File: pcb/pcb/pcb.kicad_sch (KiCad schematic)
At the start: 24 parts, among them J1 UART, J2 Barrel_Jack, J3 Stepper, SW1 RESET, SW2 FLASH, U1 ESP32-WROOM-32, U2 TSR_1-2433

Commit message: third reddit revision
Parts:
- L1: footprint Inductor_SMD:L_1206_3216Metric_Pad1.22x1.90mm_HandSolder -> Inductor_SMD:L_TracoPower_TCK-141
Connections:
- net A1: now also J3.2 (Pin_2); no longer J3.3 (Pin_3)
- net A2: now also J3.1 (Pin_1); no longer J3.4 (Pin_4)
- net B1: now also J3.3 (Pin_3); no longer J3.2 (Pin_2)
- net B2: now also J3.4 (Pin_4); no longer J3.1 (Pin_1)
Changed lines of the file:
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@@
   (title_block
     (title "twilight")
-    (date "2022-01-28")
+    (date "2022-01-30")
     (rev "1.0")
     (comment 4 "ESP32 and DRV8825 based stepper motor controller")
@@
     (property "Reference" "L1" (id 0) (at 194.31 39.37 90))
     (property "Value" "5.6uH" (id 1) (at 194.31 41.91 90))
-    (property "Footprint" "Inductor_SMD:L_1206_3216Metric_Pad1.22x1.90mm_HandSolder" (id 2) (at 194.31 45.72 0)
+    (property "Footprint" "Inductor_SMD:L_TracoPower_TCK-141" (id 2) (at 194.31 45.72 0)
       (effects (font (size 1.27 1.27)) hide)
     )
@@
     (pin "2")
   )
-  (symbol (lib_id "Connector_Generic:Conn_01x04") (at 215.9 129.54 0) (mirror x) (unit 1)
-    (in_bom yes) (on_board yes) (fields_autoplaced)
-    (property "Reference" "J3" (id 0) (at 215.9 118.11 0))
-    (property "Value" "Stepper" (id 1) (at 215.9 120.65 0))
-    (property "Footprint" "Connector_PinHeader_2.54mm:PinHeader_1x04_P2.54mm_Horizontal" (id 2) (at 215.9 129.54 0)
-      (effects (font (size 1.27 1.27)) hide)
-    )
-    (property "Datasheet" "~" (id 3) (at 215.9 129.54 0)
+  (symbol (lib_id "Connector_Generic:Conn_01x04") (at 215.9 127 0) (unit 1)
+    (in_bom yes) (on_board yes) (fields_autoplaced)
+    (property "Reference" "J3" (id 0) (at 218.44 126.9999 0)
+      (effects (font (size 1.27 1.27)) (justify left))
+    )
+    (property "Value" "Stepper" (id 1) (at 218.44 129.5399 0)
+      (effects (font (size 1.27 1.27)) (justify left))
+    )
+    (property "Footprint" "Connector_PinHeader_2.54mm:PinHeader_1x04_P2.54mm_Horizontal" (id 2) (at 215.9 127 0)
+      (effects (font (size 1.27 1.27)) hide)
+    )
+    (property "Datasheet" "~" (id 3) (at 215.9 127 0)
       (effects (font (size 1.27 1.27)) hide)
     )
@@
     )
     (path "/6243677a-61f4-42bd-9218-5496f7fcebdc"
-      (reference "L1") (unit 1) (value "5.6uH") (footprint "Inductor_SMD:L_1206_3216Metric_Pad1.22x1.90mm_HandSolder")
+      (reference "L1") (unit 1) (value "5.6uH") (footprint "Inductor_SMD:L_TracoPower_TCK-141")
     )
     (path "/618b85b8-3878-4dca-95c1-d1249ea332c0"

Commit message: fix mounting hole footprint in schematic
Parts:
- H1, H3: footprint MountingHole:MountingHole_3.2mm_M3_Pad -> MountingHole:MountingHole_3.2mm_M3
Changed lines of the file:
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@@
       (effects (font (size 1.27 1.27)) (justify left))
     )
-    (property "Footprint" "MountingHole:MountingHole_3.2mm_M3_Pad" (id 2) (at 34.29 27.94 0)
+    (property "Footprint" "MountingHole:MountingHole_3.2mm_M3" (id 2) (at 34.29 27.94 0)
       (effects (font (size 1.27 1.27)) hide)
     )
@@
       (effects (font (size 1.27 1.27)) (justify left))
     )
-    (property "Footprint" "MountingHole:MountingHole_3.2mm_M3_Pad" (id 2) (at 69.85 27.94 0)
+    (property "Footprint" "MountingHole:MountingHole_3.2mm_M3" (id 2) (at 69.85 27.94 0)
       (effects (font (size 1.27 1.27)) hide)
     )
@@
     )
     (path "/34fa3d54-c535-425c-b022-e1943d8d5f86"
-      (reference "H1") (unit 1) (value "MountingHole") (footprint "MountingHole:MountingHole_3.2mm_M3_Pad")
+      (reference "H1") (unit 1) (value "MountingHole") (footprint "MountingHole:MountingHole_3.2mm_M3")
     )
     (path "/00d9b647-6f7b-4061-b8f8-f07282eb45d6"
@@
     )
     (path "/72d1a3aa-0e7b-4b10-a84c-7a0d93e80db5"
-      (reference "H3") (unit 1) (value "MountingHole") (footprint "MountingHole:MountingHole_3.2mm_M3_Pad")
+      (reference "H3") (unit 1) (value "MountingHole") (footprint "MountingHole:MountingHole_3.2mm_M3")
     )
     (path "/b3ffd185-6873-4234-b901-27672efba3ad"

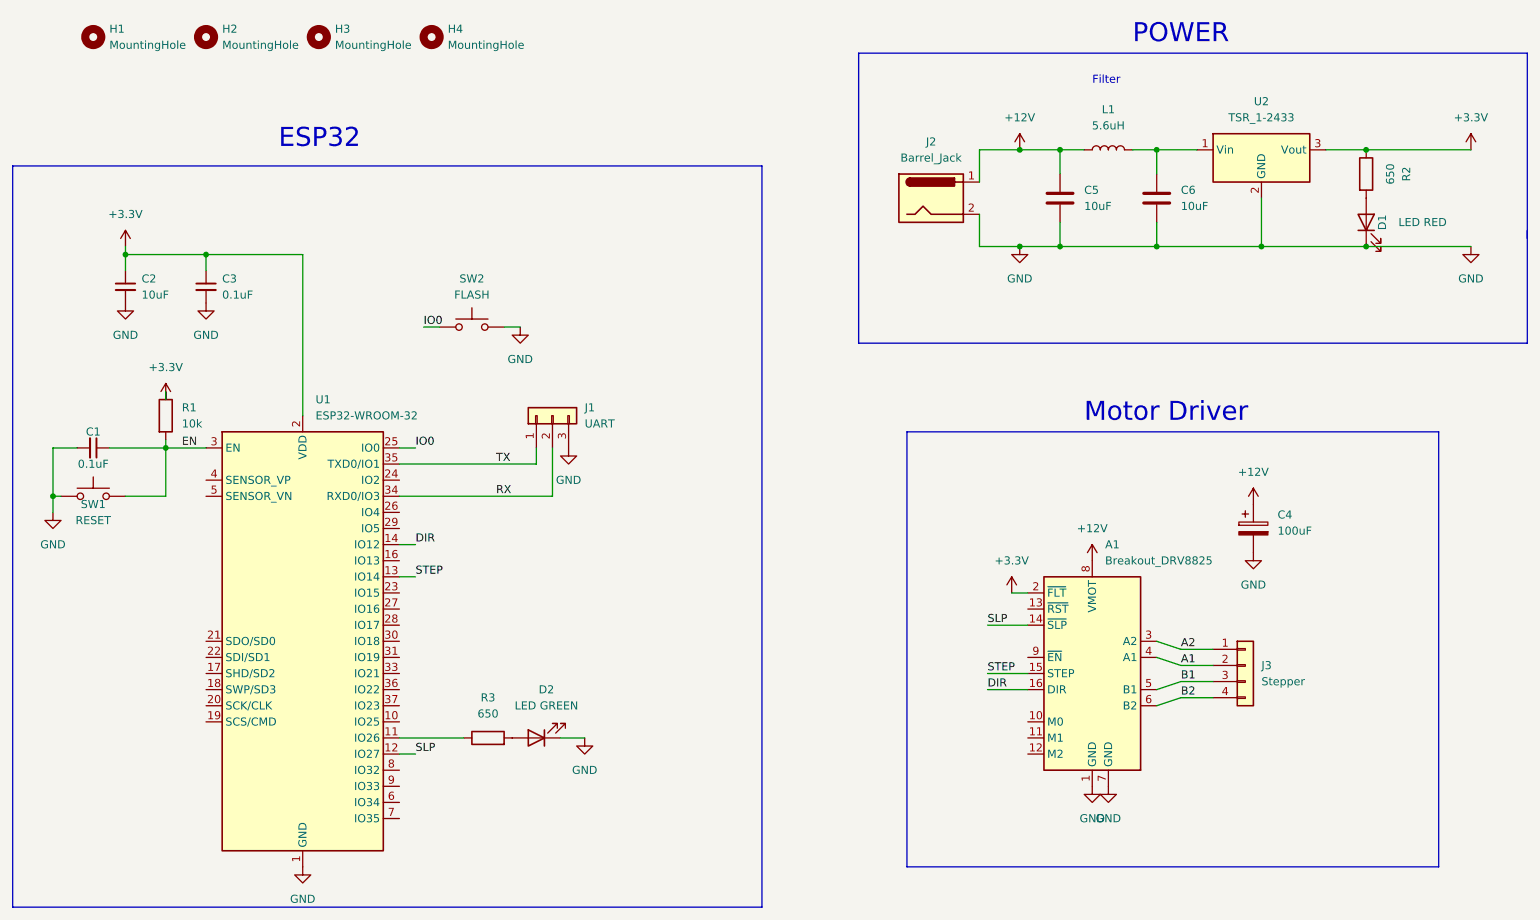
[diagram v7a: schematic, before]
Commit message: change resistor values to more standard
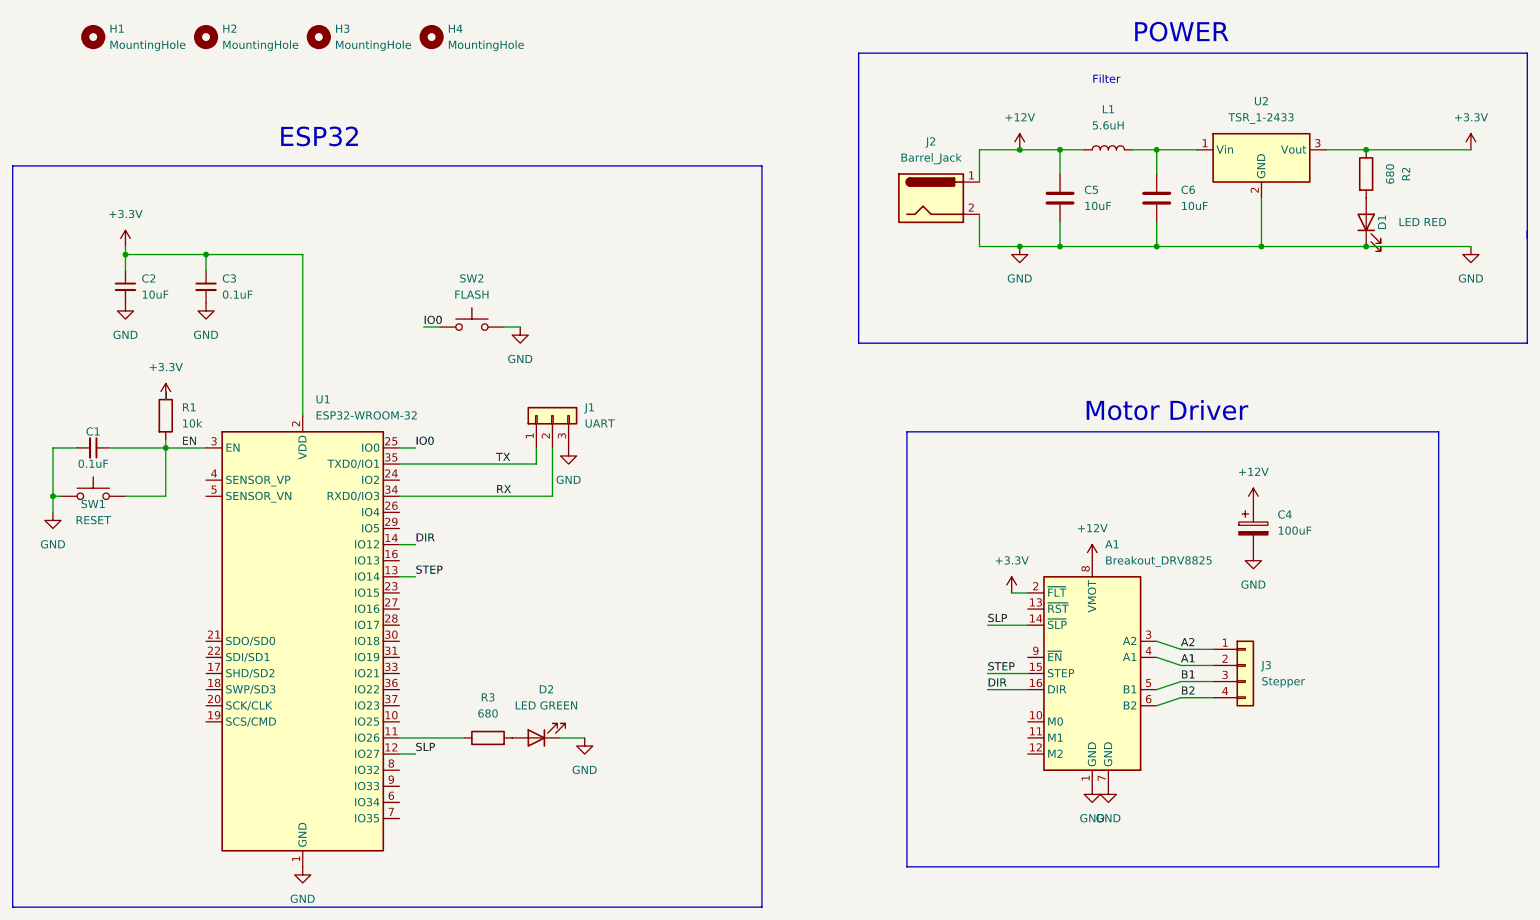
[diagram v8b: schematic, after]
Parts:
- R2, R3: value 650 -> 680
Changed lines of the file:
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@@
     (in_bom yes) (on_board yes) (fields_autoplaced)
     (property "Reference" "R3" (id 0) (at 96.52 132.08 90))
-    (property "Value" "650" (id 1) (at 96.52 134.62 90))
+    (property "Value" "680" (id 1) (at 96.52 134.62 90))
     (property "Footprint" "Resistor_SMD:R_1206_3216Metric_Pad1.30x1.75mm_HandSolder" (id 2) (at 96.52 140.208 90)
       (effects (font (size 1.27 1.27)) hide)
@@
     (in_bom yes) (on_board yes)
     (property "Reference" "R2" (id 0) (at 241.3 49.53 90))
-    (property "Value" "650" (id 1) (at 238.76 49.53 90))
+    (property "Value" "680" (id 1) (at 238.76 49.53 90))
     (property "Footprint" "Resistor_SMD:R_1206_3216Metric_Pad1.30x1.75mm_HandSolder" (id 2) (at 233.172 49.53 90)
       (effects (font (size 1.27 1.27)) hide)
@@
     )
     (path "/608f4001-cff0-46a4-9e8b-63808992aebd"
-      (reference "R2") (unit 1) (value "650") (footprint "Resistor_SMD:R_1206_3216Metric_Pad1.30x1.75mm_HandSolder")
+      (reference "R2") (unit 1) (value "680") (footprint "Resistor_SMD:R_1206_3216Metric_Pad1.30x1.75mm_HandSolder")
     )
     (path "/502f00aa-5ed9-465a-8f44-348ad78d8c9d"
-      (reference "R3") (unit 1) (value "650") (footprint "Resistor_SMD:R_1206_3216Metric_Pad1.30x1.75mm_HandSolder")
+      (reference "R3") (unit 1) (value "680") (footprint "Resistor_SMD:R_1206_3216Metric_Pad1.30x1.75mm_HandSolder")
     )
     (path "/6efe0832-cbd1-4935-befc-012d6101080a"
